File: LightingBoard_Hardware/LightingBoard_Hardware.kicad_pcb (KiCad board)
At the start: 2 copper layers, 61 x 108.8 mm, 23 parts, among them U1 LDD-1500L, U2 LDD-1500L, U3 TM4C129E_Launchpad, U4 +5V OKI

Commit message: Rev2 Probably
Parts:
- removed D4: Org_LED, LED_SMD:LED_0603_1608Metric_Pad1.05x0.95mm_HandSolder
- removed R4: 500, Resistor_SMD:R_0603_1608Metric_Pad1.05x0.95mm_HandSolder
- added D1: G_LED, LED_SMD:LED_0603_1608Metric_Pad1.05x0.95mm_HandSolder, F.Cu at (142.5, 43.6)
- D2: value G_LED -> Org_LED
- R1: value 470 -> 500
- U4: value +5V OKI -> OKI
- moved R1 20.2 mm to (138.5, 43.6)
- moved R2 8.64 mm to (147.2, 43.6)
- moved D2 8.62 mm to (151.1, 43.6)
- moved D3 8.51 mm to (159.5, 43.6)
- moved R3 8.48 mm to (155.6, 43.6)
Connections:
- Conn1 pad 2: +12VA -> Net-(C2-Pad1)
- Conn1 pad 3: Net-(C2-Pad1) -> +12VA
- Conn4 pad 2: Net-(Conn4-Pad2) -> Dout_NeoPixel
- R1 pad 1: Net-(Conn4-Pad2) -> +5V
- R1 pad 2: Dout_NeoPixel -> Net-(D1-Pad2)
- R2 pad 1: +5V -> Dout_NeoPixel
- R3 pad 1: Dout_NeoPixel -> Headlight_OnOff_PWM1
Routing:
- net Net-(C2-Pad1): track 27.1 -> 34.3 mm
- net +12VA: track 67.0 -> 72.6 mm
- net Dout_NeoPixel: track 77.7 -> 82.8 mm
- net Net-(Conn4-Pad2): track 3.30 -> 0.00 mm
- net Net-(D1-Pad2): track 0.00 -> 2.22 mm
- net Net-(D4-Pad2): track 2.16 -> 0.00 mm
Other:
- board text added: "Lighting Board, Rev.2 Mars Rover Design Team Missouri S&T, 2019 Ryan Nachtmann, John Beuke"
- board text removed: "Lighting Board, Rev.1 Mars Rover Design Team Missouri S&T, 2019 Ryan Nachtmann, John Beuke"

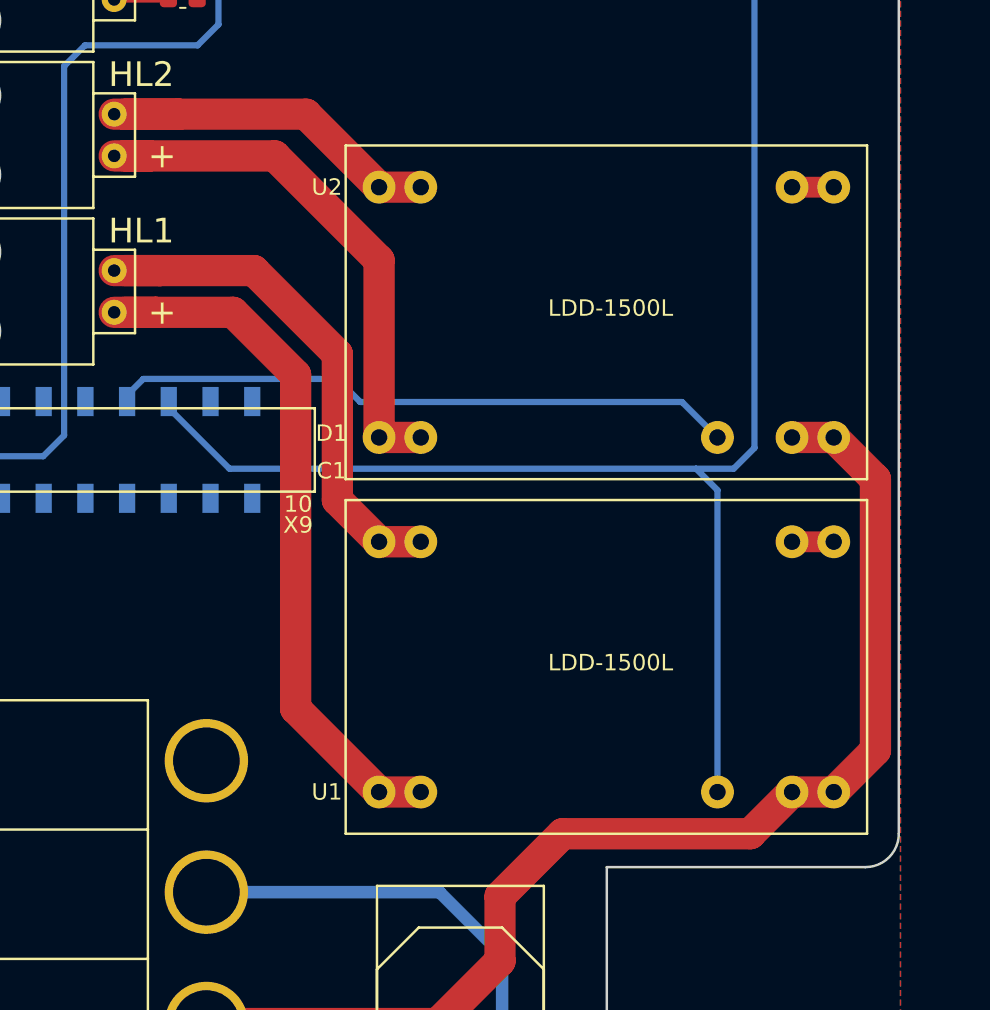
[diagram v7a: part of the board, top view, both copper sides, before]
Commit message: Rev2 Probably MK2
Shifted the LDD-1500L's up by 1.5mm
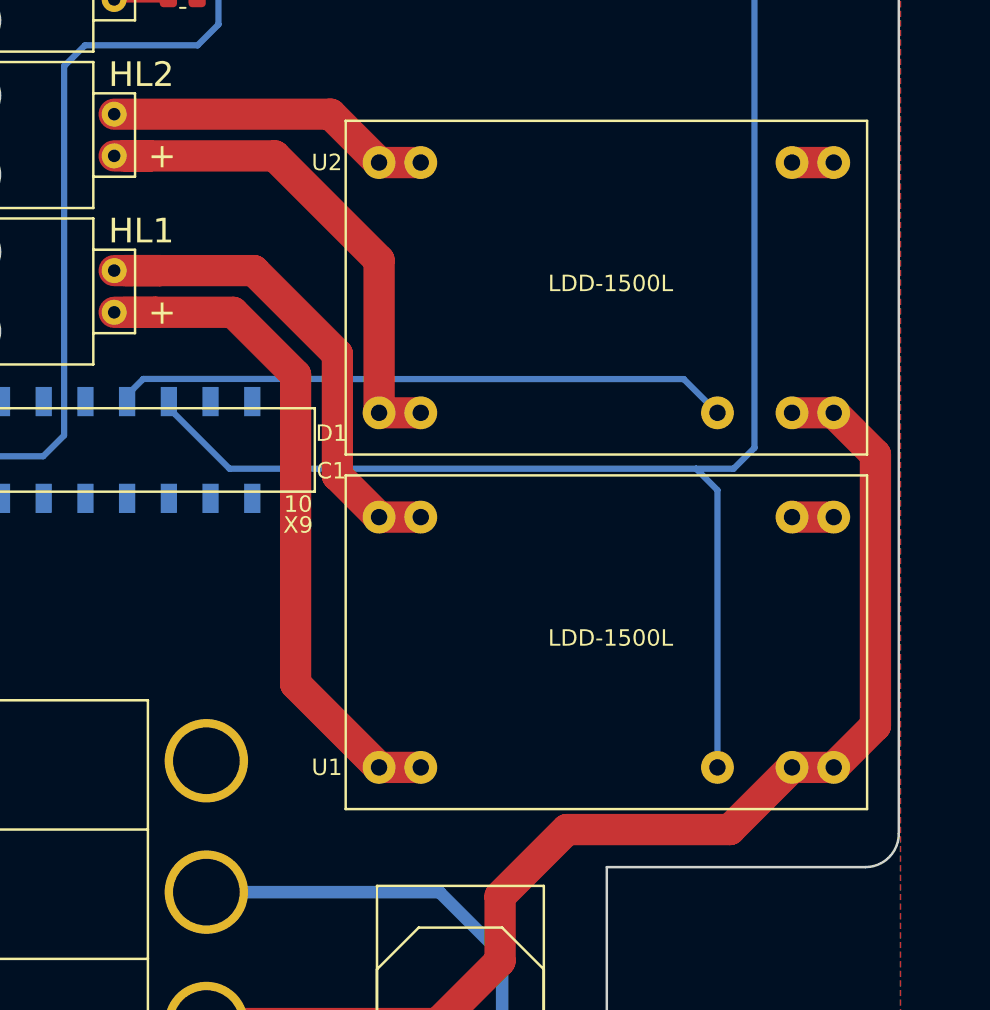
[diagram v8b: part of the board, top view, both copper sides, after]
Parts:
- moved U1 1.50 mm to (128.8, 79.4)
- moved U2 1.50 mm to (128.8, 57.8)
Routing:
- net /Headlight_V2-: track 23.8 -> 19.9 mm
- net Headlight_OnOff_PWM1: track 92.9 -> 91.4 mm
- net /Headlight_V2+: track 33.6 -> 32.1 mm
- net /Headlight_V1-: track 32.9 -> 31.4 mm
- net /Headlight_V1+: track 44.6 -> 43.1 mm
- net +12VA: track 72.6 -> 73.2 mm
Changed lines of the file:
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@@
     (thickness 1.6)
     (drawings 30)
-    (tracks 102)
+    (tracks 101)
     (zones 0)
     (modules 22)
@@
   )
   (setup
-    (last_trace_width 0.25)
+    (last_trace_width 1.905)
     (user_trace_width 0.0381)
     (user_trace_width 0.03998)
@@
   )
   (module MRDT_Devices:LDD-1500L_LED_DRIVER (layer F.Cu)
-    (at 128.778 80.899 270)
+    (at 128.778 79.399 270)
     (fp_text reference U1 (at 17.78 1.143) (layer F.SilkS)
       (effects (font (size 1 1) (thickness 0.15)))
@@
   )
   (module MRDT_Devices:LDD-1500L_LED_DRIVER (layer F.Cu)
-    (at 128.778 59.309 270)
+    (at 128.778 57.809 270)
     (fp_text reference U2 (at 2.54 1.143) (layer F.SilkS)
       (effects (font (size 1 1) (thickness 0.15)))
@@
   (segment (start 112.776 48.514) (end 104.013 48.514) (width 0.762) (layer B.Cu) (net 1))
   (segment (start 117.983 50.419) (end 114.681 50.419) (width 0.381) (layer F.Cu) (net 1))
-  (segment (start 158.496 83.439) (end 155.956 83.439) (width 1.27) (layer F.Cu) (net 2))
-  (segment (start 158.496 61.849) (end 155.956 61.849) (width 1.27) (layer F.Cu) (net 2))
+  (segment (start 155.956 60.349) (end 158.496 60.349) (width 1.905) (layer F.Cu) (net 2))
+  (segment (start 155.956 81.939) (end 158.496 81.939) (width 1.905) (layer F.Cu) (net 2))
   (segment (start 138.303 123.317) (end 138.303 119.634) (width 0.381) (layer F.Cu) (net 3))
   (segment (start 138.303 119.634) (end 138.303 108.585) (width 0.762) (layer B.Cu) (net 3))
@@
   (segment (start 134.492 104.776) (end 120.2944 104.776) (width 0.762) (layer B.Cu) (net 3))
   (segment (start 134.493 104.775) (end 134.492 104.776) (width 0.762) (layer B.Cu) (net 3))
-  (segment (start 141.986 101.219) (end 153.416 101.219) (width 1.905) (layer F.Cu) (net 4))
-  (segment (start 153.416 101.219) (end 155.956 98.679) (width 1.905) (layer F.Cu) (net 4))
-  (segment (start 155.956 98.679) (end 158.496 98.679) (width 1.905) (layer F.Cu) (net 4))
-  (segment (start 158.496 98.679) (end 161.036 96.139) (width 1.905) (layer F.Cu) (net 4))
-  (segment (start 161.036 96.139) (end 161.036 79.629) (width 1.905) (layer F.Cu) (net 4))
-  (segment (start 161.036 79.629) (end 158.496 77.089) (width 1.905) (layer F.Cu) (net 4))
-  (segment (start 158.496 77.089) (end 155.956 77.089) (width 1.905) (layer F.Cu) (net 4))
-  (segment (start 141.986 101.219) (end 138.176 105.029) (width 1.905) (layer F.Cu) (net 4))
+  (segment (start 134.365 112.775) (end 120.2944 112.775) (width 1.905) (layer F.Cu) (net 4))
+  (segment (start 152.17 100.965) (end 142.24 100.965) (width 1.905) (layer F.Cu) (net 4))
+  (segment (start 155.956 97.179) (end 152.17 100.965) (width 1.905) (layer F.Cu) (net 4))
+  (segment (start 142.24 100.965) (end 138.176 105.029) (width 1.905) (layer F.Cu) (net 4))
   (segment (start 138.176 105.029) (end 138.176 108.966) (width 1.905) (layer F.Cu) (net 4))
   (segment (start 138.176 108.966) (end 134.366 112.776) (width 1.905) (layer F.Cu) (net 4))
-  (segment (start 134.365 112.775) (end 120.2944 112.775) (width 1.905) (layer F.Cu) (net 4))
   (segment (start 134.366 112.776) (end 134.365 112.775) (width 1.905) (layer F.Cu) (net 4))
-  (segment (start 130.81 98.679) (end 125.73 93.599) (width 1.905) (layer F.Cu) (net 5))
-  (segment (start 125.73 93.599) (end 125.73 73.279) (width 1.905) (layer F.Cu) (net 5))
+  (segment (start 155.956 75.589) (end 158.496 75.589) (width 1.905) (layer F.Cu) (net 4))
+  (segment (start 155.956 97.179) (end 158.496 97.179) (width 1.905) (layer F.Cu) (net 4))
+  (segment (start 158.496 75.589) (end 161.036 78.129) (width 1.905) (layer F.Cu) (net 4))
+  (segment (start 161.036 94.639) (end 158.496 97.179) (width 1.905) (layer F.Cu) (net 4))
+  (segment (start 161.036 78.129) (end 161.036 94.639) (width 1.905) (layer F.Cu) (net 4))
   (segment (start 125.73 73.279) (end 121.92 69.469) (width 1.905) (layer F.Cu) (net 5))
-  (segment (start 130.81 98.679) (end 133.35 98.679) (width 1.905) (layer F.Cu) (net 5))
   (segment (start 114.681 69.469) (end 117.221 69.469) (width 1.905) (layer F.Cu) (net 5))
   (segment (start 121.92 69.469) (end 117.221 69.469) (width 1.905) (layer F.Cu) (net 5))
   (segment (start 117.221 69.469) (end 115.316 69.469) (width 1.905) (layer F.Cu) (net 5))
-  (segment (start 130.81 83.439) (end 133.35 83.439) (width 1.905) (layer F.Cu) (net 6))
-  (segment (start 128.27 80.899) (end 130.81 83.439) (width 1.905) (layer F.Cu) (net 6))
-  (segment (start 128.27 72.009) (end 128.27 80.899) (width 1.905) (layer F.Cu) (net 6))
+  (segment (start 130.81 97.179) (end 125.73 92.099) (width 1.905) (layer F.Cu) (net 5))
+  (segment (start 125.73 92.099) (end 125.73 73.279) (width 1.905) (layer F.Cu) (net 5))
+  (segment (start 130.81 97.179) (end 133.35 97.179) (width 1.905) (layer F.Cu) (net 5))
   (segment (start 123.19 66.929) (end 128.27 72.009) (width 1.905) (layer F.Cu) (net 6))
   (segment (start 114.681 66.929) (end 117.475 66.929) (width 1.905) (layer F.Cu) (net 6))
   (segment (start 115.316 66.929) (end 117.475 66.929) (width 1.905) (layer F.Cu) (net 6))
   (segment (start 117.475 66.929) (end 123.19 66.929) (width 1.905) (layer F.Cu) (net 6))
-  (segment (start 133.35 61.849) (end 130.81 61.849) (width 1.905) (layer F.Cu) (net 7))
-  (segment (start 130.81 61.849) (end 126.365 57.404) (width 1.905) (layer F.Cu) (net 7))
-  (segment (start 114.681 57.404) (end 118.618 57.404) (width 1.905) (layer F.Cu) (net 7))
-  (segment (start 126.365 57.404) (end 118.618 57.404) (width 1.905) (layer F.Cu) (net 7))
-  (segment (start 118.618 57.404) (end 115.316 57.404) (width 1.905) (layer F.Cu) (net 7))
-  (segment (start 133.35 77.089) (end 130.81 77.089) (width 1.905) (layer F.Cu) (net 8))
-  (segment (start 130.81 77.089) (end 130.81 66.294) (width 1.905) (layer F.Cu) (net 8))
+  (segment (start 130.81 81.939) (end 128.27 79.399) (width 1.905) (layer F.Cu) (net 6))
+  (segment (start 128.27 79.399) (end 128.27 72.009) (width 1.905) (layer F.Cu) (net 6))
+  (segment (start 130.81 81.939) (end 133.35 81.939) (width 1.905) (layer F.Cu) (net 6))
+  (segment (start 130.81 60.349) (end 127.865 57.404) (width 1.905) (layer F.Cu) (net 7))
+  (segment (start 127.865 57.404) (end 114.681 57.404) (width 1.905) (layer F.Cu) (net 7))
+  (segment (start 130.81 60.349) (end 133.35 60.349) (width 1.905) (layer F.Cu) (net 7))
   (segment (start 130.81 66.294) (end 124.46 59.944) (width 1.905) (layer F.Cu) (net 8))
   (segment (start 114.681 59.944) (end 116.84 59.944) (width 1.905) (layer F.Cu) (net 8))
   (segment (start 124.46 59.944) (end 116.84 59.944) (width 1.905) (layer F.Cu) (net 8))
   (segment (start 116.84 59.944) (end 115.316 59.944) (width 1.905) (layer F.Cu) (net 8))
-  (segment (start 156.464 43.561) (end 158.623 43.561) (width 0.381) (layer F.Cu) (net 48))
+  (segment (start 130.81 75.589) (end 130.81 66.294) (width 1.905) (layer F.Cu) (net 8))
+  (segment (start 130.81 75.589) (end 133.35 75.589) (width 1.905) (layer F.Cu) (net 8))
   (segment (start 146.205 43.561) (end 146.205 46.581) (width 0.381) (layer F.Cu) (net 9))
   (segment (start 146.205 46.581) (end 144.907 47.879) (width 0.381) (layer F.Cu) (net 9))
@@
   (segment (start 153.67 77.724) (end 152.4 78.994) (width 0.381) (layer B.Cu) (net 10))
   (segment (start 152.4 78.994) (end 150.114 78.994) (width 0.381) (layer B.Cu) (net 10))
-  (segment (start 151.416 98.679) (end 151.416 80.296) (width 0.381) (layer B.Cu) (net 10))
   (segment (start 151.416 80.296) (end 150.114 78.994) (width 0.381) (layer B.Cu) (net 10))
+  (segment (start 151.416 80.296) (end 151.416 97.179) (width 0.381) (layer B.Cu) (net 10))
   (segment (start 115.468001 74.903601) (end 115.468001 75.297301) (width 0.381) (layer B.Cu) (net 11))
-  (segment (start 149.257 74.93) (end 151.416 77.089) (width 0.381) (layer B.Cu) (net 11))
-  (segment (start 129.667 74.93) (end 149.257 74.93) (width 0.381) (layer B.Cu) (net 11))
-  (segment (start 128.262951 73.525951) (end 129.667 74.93) (width 0.381) (layer B.Cu) (net 11))
-  (segment (start 116.451951 73.525951) (end 128.262951 73.525951) (width 0.381) (layer B.Cu) (net 11))
   (segment (start 115.468001 74.509901) (end 116.451951 73.525951) (width 0.381) (layer B.Cu) (net 11))
   (segment (start 115.468001 74.903601) (end 115.468001 74.509901) (width 0.381) (layer B.Cu) (net 11))
+  (segment (start 151.416 75.589) (end 149.36 73.533) (width 0.381) (layer B.Cu) (net 11))
+  (segment (start 128.023049 73.533) (end 128.016 73.525951) (width 0.381) (layer B.Cu) (net 11))
+  (segment (start 149.36 73.533) (end 128.023049 73.533) (width 0.381) (layer B.Cu) (net 11))
+  (segment (start 116.451951 73.525951) (end 128.016 73.525951) (width 0.381) (layer B.Cu) (net 11))
+  (segment (start 128.016 73.525951) (end 128.262951 73.525951) (width 0.381) (layer B.Cu) (net 11))
   (segment (start 139.418 43.561) (end 141.633 43.561) (width 0.381) (layer F.Cu) (net 46))
   (segment (start 147.955 43.561) (end 150.114 43.561) (width 0.381) (layer F.Cu) (net 47))
+  (segment (start 156.464 43.561) (end 158.623 43.561) (width 0.381) (layer F.Cu) (net 48))
   (zone (net 2) (net_name GND) (layer B.Cu) (hatch edge 0.508)
     (connect_pads yes (clearance 0.508))
